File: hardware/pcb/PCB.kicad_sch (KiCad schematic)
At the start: 44 parts, among them J1 USB_A, J2 AudioJack3, J3 USB_B_Micro, Q1 BSS138, Q2 S8050, Q3 S8050, SW1 SW_RESET, SW2 S4_SW, U1 ESP32-S3-WROOM-1, U2 LM3525M-H, U3 D52Q, U4 CP2102N-Axx-xQFN24, U5 AP7361C-33E, U6 SP0506BAATG

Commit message: tweaks
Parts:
- U5: footprint Package_TO_SOT_SMD:SOT-223-3_TabPin2 -> Package_TO_SOT_SMD:SOT-223
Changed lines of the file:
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@@
     (property "Reference" "U5" (id 0) (at 134.62 177.8 0))
     (property "Value" "AP7361C-33E" (id 1) (at 134.62 180.34 0))
-    (property "Footprint" "Package_TO_SOT_SMD:SOT-223-3_TabPin2" (id 2) (at 134.62 179.705 0)
+    (property "Footprint" "Package_TO_SOT_SMD:SOT-223" (id 2) (at 134.62 179.705 0)
       (effects (font (size 1.27 1.27) italic) hide)
     )
@@
     )
     (path "/7256d11a-14ff-445c-a438-bcd70efc9185"
-      (reference "U5") (unit 1) (value "AP7361C-33E") (footprint "Package_TO_SOT_SMD:SOT-223-3_TabPin2")
+      (reference "U5") (unit 1) (value "AP7361C-33E") (footprint "Package_TO_SOT_SMD:SOT-223")
     )
     (path "/ac99ef1b-ad4b-44a0-888a-006344fe47f5"

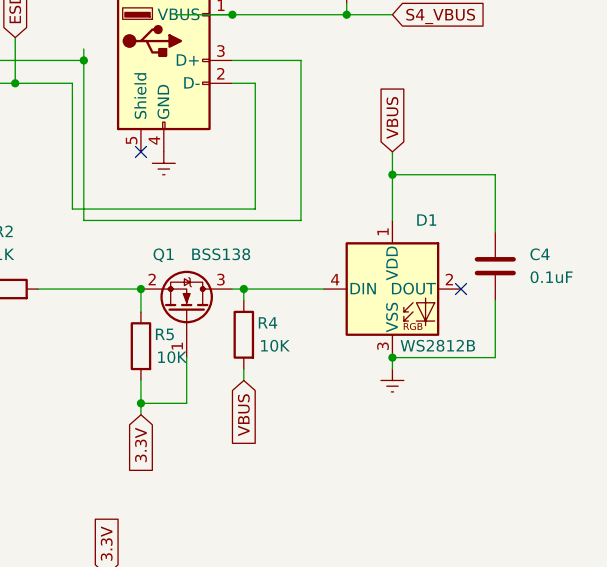
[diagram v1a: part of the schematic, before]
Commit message: swap led part#
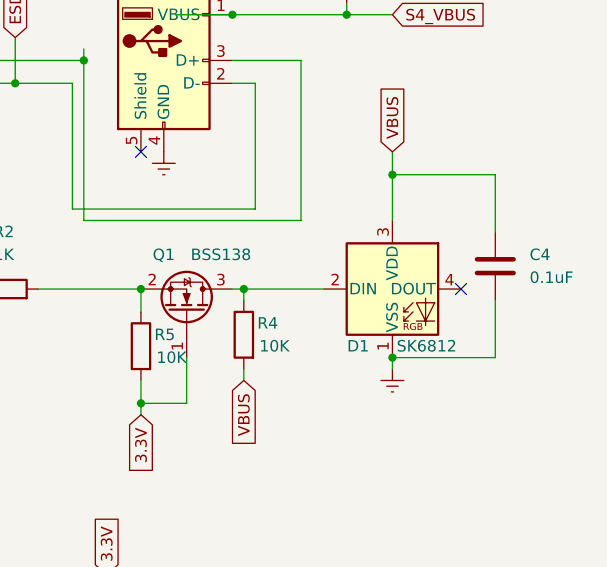
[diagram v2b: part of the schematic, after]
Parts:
- removed D1: WS2812B, LED_SMD:LED_WS2812B_PLCC4_5.0x5.0mm_P3.2mm, symbol LED:WS2812B
- added D1: SK6812, LED_SMD:LED_SK6812_PLCC4_5.0x5.0mm_P3.2mm, symbol LED:SK6812
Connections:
- net Earth: now also D1.1 (VSS)
- net VBUS: now also D1.3 (VDD)
- net at Q1.3 (D), R4.1: now also D1.2 (DIN)
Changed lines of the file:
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@@
   (junction (at 27.94 93.98) (diameter 0) (color 0 0 0 0)
   )
+  (junction (at 246.38 64.77) (diameter 0) (color 0 0 0 0)
+  )
   (junction (at 33.02 63.5) (diameter 0) (color 0 0 0 0)
   )
@@
   )
   (junction (at 53.34 154.94) (diameter 0) (color 0 0 0 0)
-  )
-  (junction (at 246.38 64.77) (diameter 0) (color 0 0 0 0)
   )
   (junction (at 191.77 93.98) (diameter 0) (color 0 0 0 0)
@@
     (pin "2")
   )
-  (symbol (lib_id "LED:WS2812B") (at 246.38 57.15 0) (unit 1)
-    (in_bom yes) (on_board yes)
-    (property "Reference" "D1" (id 0) (at 250.19 49.53 0))
-    (property "Value" "WS2812B" (id 1) (at 251.46 63.5 0))
-    (property "Footprint" "LED_SMD:LED_WS2812B_PLCC4_5.0x5.0mm_P3.2mm" (id 2) (at 247.65 64.77 0)
-      (effects (font (size 1.27 1.27)) (justify left top) hide)
-    )
-    (property "Datasheet" "https://cdn-shop.adafruit.com/datasheets/WS2812B.pdf" (id 3) (at 248.92 66.675 0)
-      (effects (font (size 1.27 1.27)) (justify left top) hide)
-    )
-    (pin "1")
-    (pin "2")
-    (pin "3")
-    (pin "4")
-  )
   (symbol (lib_id "Connector:AudioJack3") (at 45.72 73.66 0) (mirror x) (unit 1)
     (in_bom yes) (on_board yes)
@@
     (pin "2")
     (pin "3")
+  )
+  (symbol (lib_id "LED:SK6812") (at 246.38 57.15 0) (unit 1)
+    (in_bom yes) (on_board yes)
+    (property "Reference" "D1" (id 0) (at 242.57 63.5 0))
+    (property "Value" "SK6812" (id 1) (at 250.19 63.5 0))
+    (property "Footprint" "LED_SMD:LED_SK6812_PLCC4_5.0x5.0mm_P3.2mm" (id 2) (at 247.65 64.77 0)
+      (effects (font (size 1.27 1.27)) (justify left top) hide)
+    )
+    (property "Datasheet" "https://cdn-shop.adafruit.com/product-files/1138/SK6812+LED+datasheet+.pdf" (id 3) (at 248.92 66.675 0)
+      (effects (font (size 1.27 1.27)) (justify left top) hide)
+    )
+    (pin "1")
+    (pin "2")
+    (pin "3")
+    (pin "4")
   )
   (symbol (lib_id "Device:R") (at 118.11 147.32 90) (unit 1)
@@
       (reference "C15") (unit 1) (value "4.7uF") (footprint "Capacitor_SMD:C_0603_1608Metric_Pad1.08x0.95mm_HandSolder")
     )
-    (path "/2e435b0f-671e-4da0-9b1a-48c487e95e18"
-      (reference "D1") (unit 1) (value "WS2812B") (footprint "LED_SMD:LED_WS2812B_PLCC4_5.0x5.0mm_P3.2mm")
+    (path "/7437b41b-d18a-408f-a04e-b9dbafcc6f80"
+      (reference "D1") (unit 1) (value "SK6812") (footprint "LED_SMD:LED_SK6812_PLCC4_5.0x5.0mm_P3.2mm")
     )
     (path "/302a696a-e598-44f8-b7fc-984d24197d4c"

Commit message: board updates
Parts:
- removed Q2, Q3: S8050, Package_TO_SOT_SMD:SOT-23, symbol Transistor_BJT:S8050
- added Q2, Q3: MMBT3904, Package_TO_SOT_SMD:SOT-23, symbol Transistor_BJT:MMBT3904
- R3, R6: value 10k -> 10K
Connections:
- net BOOT: now also Q2.3 (C)
- net CHIP_PU: now also Q3.3 (C)
- net ESD_VBUS: now also D2.2 (A); no longer D2.1 (K)
- net U0_RXD: now also U4.21 (TXD); no longer U4.20 (RXD)
- net U0_TXD: now also U4.20 (RXD); no longer U4.21 (TXD)
- net VBUS: now also D2.1 (K); no longer D2.2 (A)
- net at R8.1, U4.19 (~{RTS}): now also Q3.2 (E)
- net at R11.2: now also Q3.1 (B)
- net at R11.1, U4.23 (~{DTR}): now also Q2.2 (E)
- net at R8.2: now also Q2.1 (B)
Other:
- moved on the sheet: D2, J2, R6

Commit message: Revision 2: Fixed auto program transistor pins Fixed TX/RX to U0 Increased board size Added screw holes Added BOOT switch Added RESET jumper
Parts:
- added C16: 0.1uF, Capacitor_SMD:C_0603_1608Metric_Pad1.08x0.95mm_HandSolder, symbol Device:C
- added SW3: BOOT, Button_Switch_SMD:SW_Push_1P1T_NO_6x6mm_H9.5mm, symbol Switch:SW_Push
- added SW4: RESET, Connector_PinHeader_2.54mm:PinHeader_1x02_P2.54mm_Vertical, symbol Switch:SW_Push
- SW1: value SW_RESET -> RESET
- SW2: value S4_SW -> S4
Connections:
- net BOOT: now also C16.1, SW3.2
- net CHIP_PU: now also SW4.2
- net Earth: now also C16.2, SW3.1, SW4.1
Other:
- moved on the sheet: C2, SW1

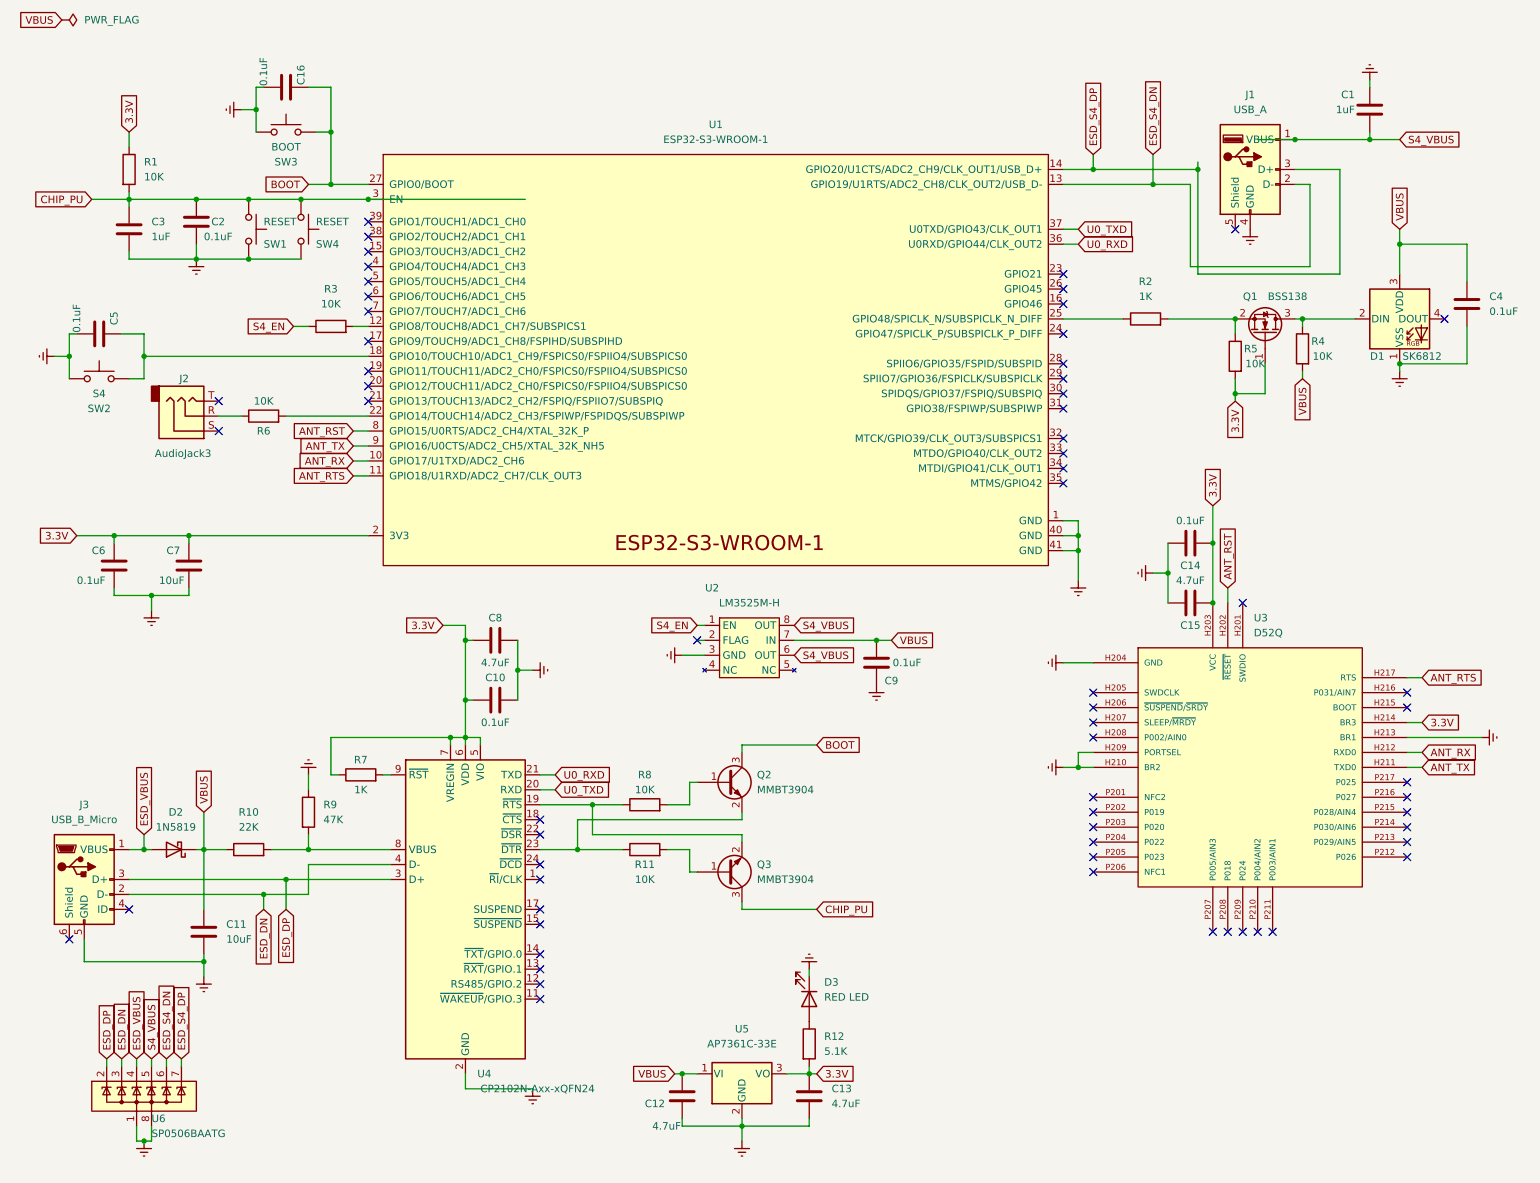
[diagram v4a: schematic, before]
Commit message: Earth to GND
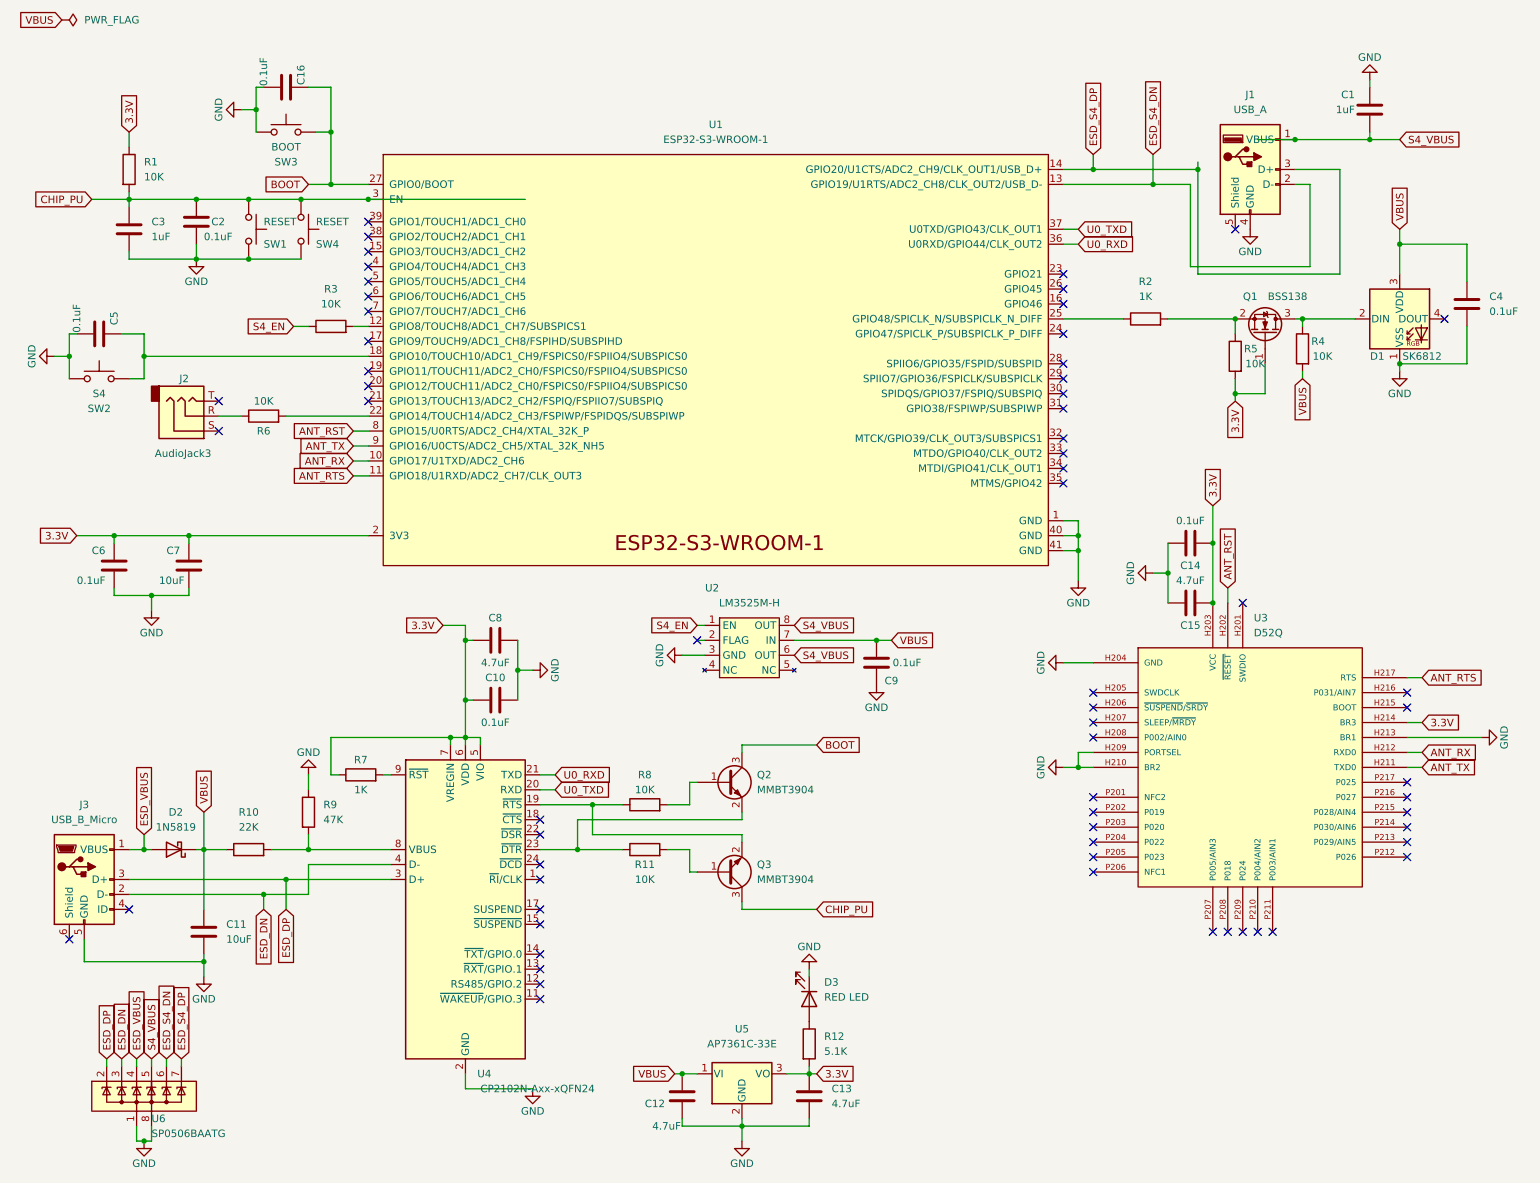
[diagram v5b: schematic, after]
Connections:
- net Earth renamed GND

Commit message: fix 3d models
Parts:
- SW2, SW4: footprint Connector_PinHeader_2.54mm:PinHeader_1x02_P2.54mm_Vertical -> Connector_JST:JST_XH_B2B-XH-A_1x02_P2.50mm_Vertical
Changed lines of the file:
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@@
       (effects (font (size 1.27 1.27)) (justify left))
     )
-    (property "Footprint" "Connector_PinHeader_2.54mm:PinHeader_1x02_P2.54mm_Vertical" (id 2) (at 64.77 41.91 0)
+    (property "Footprint" "Connector_JST:JST_XH_B2B-XH-A_1x02_P2.50mm_Vertical" (id 2) (at 64.77 41.91 0)
       (effects (font (size 1.27 1.27)) hide)
     )
@@
     (property "Reference" "SW2" (id 0) (at 25.4 72.39 0))
     (property "Value" "S4" (id 1) (at 25.4 69.85 0))
-    (property "Footprint" "Connector_PinHeader_2.54mm:PinHeader_1x02_P2.54mm_Vertical" (id 2) (at 25.4 62.23 0)
+    (property "Footprint" "Connector_JST:JST_XH_B2B-XH-A_1x02_P2.50mm_Vertical" (id 2) (at 25.4 62.23 0)
       (effects (font (size 1.27 1.27)) hide)
     )
@@
     )
     (path "/761492e2-a989-4596-80c3-fcd6943df072"
-      (reference "SW2") (unit 1) (value "S4") (footprint "Connector_PinHeader_2.54mm:PinHeader_1x02_P2.54mm_Vertical")
+      (reference "SW2") (unit 1) (value "S4") (footprint "Connector_JST:JST_XH_B2B-XH-A_1x02_P2.50mm_Vertical")
     )
     (path "/39878562-d955-4b7e-bbe7-a787f143b36a"
@@
     )
     (path "/00e0a510-b77b-4e90-ac6f-b11958449141"
-      (reference "SW4") (unit 1) (value "RESET") (footprint "Connector_PinHeader_2.54mm:PinHeader_1x02_P2.54mm_Vertical")
+      (reference "SW4") (unit 1) (value "RESET") (footprint "Connector_JST:JST_XH_B2B-XH-A_1x02_P2.50mm_Vertical")
     )
     (path "/901fa854-b4f7-4cd6-81a2-bc814b2d6c79"
